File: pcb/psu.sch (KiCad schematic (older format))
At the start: 8 parts, among them J1 CONN_INTEGRALSTICK_FPGA_DEVICE, J2 CONN_INTEGRALSTICK_MCU_DEVICE, U1 STM32F777NIH6‎, U2 XC7A50T-1FTG256C, U7 LTC3374-QFN

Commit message: Finished initial schematic. Pin assignments will likely change during routing. Ready for test point insertion and signoff review.
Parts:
- added C107, C114, C117: 47 uF, symbol device:C
- added C108, C109, C110, C112: 22 uF, symbol device:C
- added C111, C113, C115: 10 uF, symbol device:C
- added C116: 100 uF, symbol device:C
- added L1: SPM6530T-2R2M, symbol passive-azonenberg:INDUCTOR_PWROUT
- added L2: NR6028T2R2N, symbol passive-azonenberg:INDUCTOR_PWROUT
- added L3, L4, L5: NRS5030T2R2NMGJ, symbol passive-azonenberg:INDUCTOR_PWROUT
- added R26: 1K, symbol device:R
- added R29, R30, R31, R32, R33: 0, symbol device:R
- added R34: 255K, symbol device:R
- added R35: 232K, symbol device:R
- added R36: 806K, symbol device:R
- added R37, R38, R39: 1.02M, symbol device:R
- added R40: 464K, symbol device:R
- added R41: 649K, symbol device:R
- added R42: 475K, symbol device:R
- added R43: 324K, symbol device:R
- added TP2, TP3: TESTPAD, symbol conn:CONN_01X01
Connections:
- net 1V0: now also C116.1, L1.1, R29.2
- net 1V8: now also C110.1, L4.1, R31.2
- net 2V5: now also C108.1, L5.1, R32.2
- net 3V3: now also C114.1, L2.1, R26.1, R33.2
- net 5V0: now also U7.11 (VIN4), U7.13 (EN4), U7.17 (RT), U7.18 (EN6), U7.2 (VIN1), U7.20 (FB5), U7.21 (VIN5), U7.24 (VIN6), U7.27 (VIN7), U7.30 (VIN8), U7.32 (EN8), U7.33 (EN7), U7.34 (MODE), U7.35 (VCC), U7.38 (EN1), U7.5 (VIN2), U7.6 (FB2), U7.7 (FB3), U7.8 (VIN3), C107.1, C109.1, C111.1, C113.1, C115.1, C117.1
- net GND: now also U7.14 (EN3), U7.16 (SYNC), U7.19 (EN5), U7.37 (EN2), U7.PAD (GND), C107.2, C108.2, C109.2, C110.2, C111.2, C112.2, C113.2, C114.2, C115.2, C116.2, C117.2, R39.1, R40.1, R41.1, R42.1, R43.1
- net 1V0_FB: now reaches U7.1 (FB1)
- net 1V0_FB: now also R34.1, R39.2
- net 1V0_SW: now reaches U7.3 (SW1)
- net 1V0_SW: now also U7.4 (SW2), U7.9 (SW3), L1.2
- net 3V3_SW: now reaches U7.10 (SW4)
- net 3V3_SW: now also U7.22 (SW5), L2.2
- net 3V3_FB: now reaches U7.12 (FB4)
- net 3V3_FB: now also R38.1, R43.2
- net 1V2_SW: now reaches U7.23 (SW6)
- net 1V2_SW: now also L3.2
- net 1V2_FB: now reaches U7.25 (FB6)
- net 1V2_FB: now also R35.1, R40.2
- net 1V8_FB: now reaches U7.26 (FB7)
- net 1V8_FB: now also R36.1, R41.2
- net 1V8_SW: now reaches U7.28 (SW7)
- net 1V8_SW: now also L4.2
- net 2V5_SW: now reaches U7.29 (SW8)
- net 2V5_SW: now also L5.2
- net 2V5_FB: now reaches U7.31 (FB8)
- net 2V5_FB: now also R37.1, R42.2
- net PGOOD: now reaches U7.15 (PGOOD_ALL)
- net PGOOD: now also R26.2, TP2.1 (P1)
- net PSU_TEMP: now reaches U7.36 (TEMP)
- net PSU_TEMP: now also TP3.1 (P1)
- new net 1V0_SENSE: R29.1, R34.2
- new net 1V2: C112.1, L3.1, R30.2
- new net 1V2_SENSE: R30.1, R35.2
- new net 1V8_SENSE: R31.1, R36.2
- new net 2V5_SENSE: R32.1, R37.2
- new net 3V3_SENSE: R33.1, R38.2
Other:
- note added: "PCB bulk input cap (reduce input ripple)"
- note added: "Remote sense and feedback for power rails"
- note added: "SMPS input caps"
- note added: "SMPS output caps"
- note added: "for 1V0"
- note added: "for 1V2"
- note added: "for 1V8"
- note added: "for 2V5"
- note added: "for 3V3"
- note removed: "TODO: SMPS stuff"

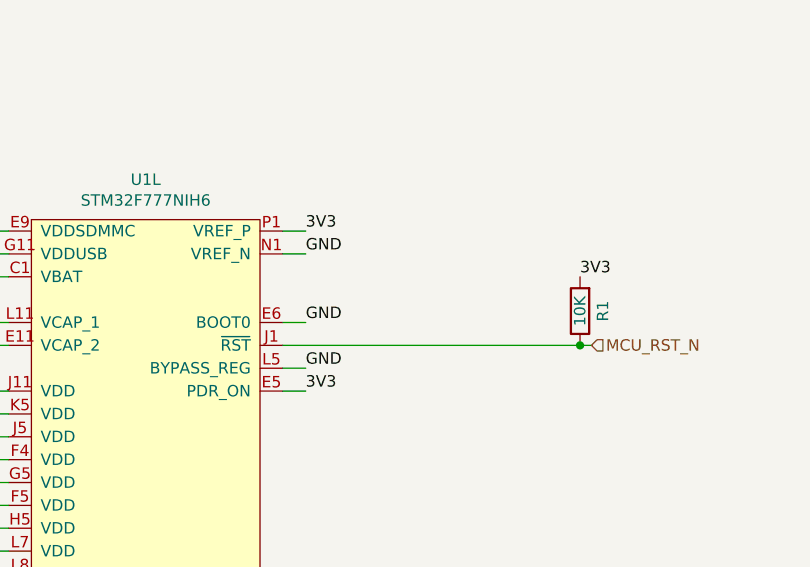
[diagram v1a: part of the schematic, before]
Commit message: Added pulldown to BOOT0 on MCU, brought it out to previously unused connector pin
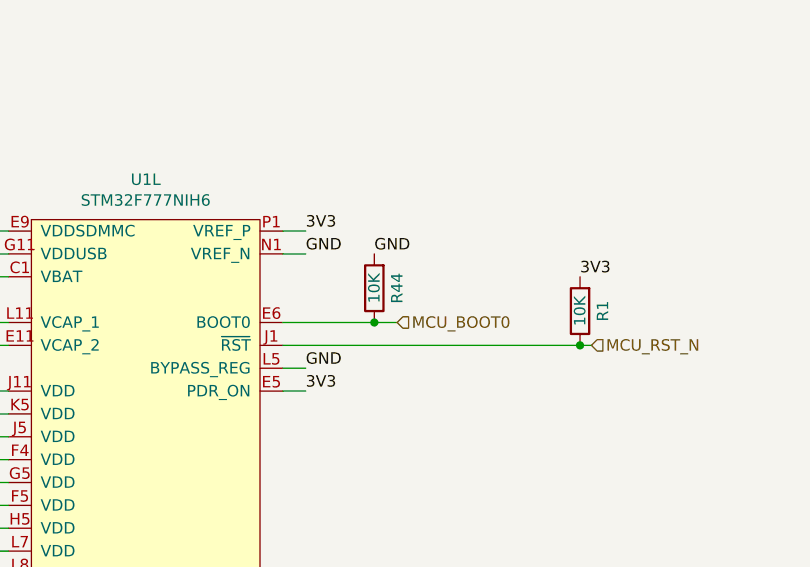
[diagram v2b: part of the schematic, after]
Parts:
- added R44: 10K, symbol device:R
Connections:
- net GND: now also R44.2; no longer U1.E6 (BOOT0)
- new net MCU_BOOT0: R44.1, U1.E6 (BOOT0)
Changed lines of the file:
@@
 Wire Wire Line
 	8400 8050 8300 8050
-Text Label 8400 8350 0    50   ~ 0
-GND
 Text HLabel 9650 8450 2    50   Input ~ 0
 MCU_RST_N
@@
 Text Label 8400 8650 0    50   ~ 0
 3V3
-Wire Wire Line
-	8400 8350 8300 8350
 Wire Wire Line
 	8400 8550 8300 8550
@@
 Wire Wire Line
 	7700 3300 7100 3300
+Text HLabel 8800 8350 2    50   Input ~ 0
+MCU_BOOT0
+$Comp
+L device:R R44
+U 1 1 5CFC62C6
+P 8700 8200
+F 0 "R44" V 8600 8200 50  0000 C CNN
+F 1 "10K" V 8700 8200 50  0000 C CNN
+F 2 "" V 8630 8200 50  0001 C CNN
+F 3 "" H 8700 8200 50  0001 C CNN
+	1    8700 8200
+	-1   0    0    1
+$EndComp
+Wire Wire Line
+	8300 8350 8700 8350
+Connection ~ 8700 8350
+Wire Wire Line
+	8700 8350 8800 8350
+Text Label 8700 8050 0    50   ~ 0
+GND
 $EndSCHEMATC

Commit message: Added capacitor for bbRAM on STM32. Removed MCU config oscillator, we now use the FPGA or internal oscillator as clock. Added SPI bus from FPGA to MCU.
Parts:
- added C46: CPH3225A-2K, symbol device:CP1
- added D2: CTS520,L3F‎, symbol device:D_Schottky
- added R45: 330, symbol device:R
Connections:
- net 3V3: now also D2.2 (A); no longer U1.C1 (VBAT)
- net GND: now also C46.2
- new net: D2.1 (K), R45.1
- new net MCU_VBAT: C46.1, R45.2, U1.C1 (VBAT)
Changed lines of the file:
@@
 Wire Wire Line
 	7000 7950 7100 7950
-Wire Wire Line
-	7000 8150 7100 8150
 $Comp
 L device:C C1
@@
 Wire Wire Line
 	7000 7950 7000 8050
-Connection ~ 7000 8050
-Wire Wire Line
-	7000 8050 7000 8150
 $Comp
 L device:C C2
@@
 Text Label 8700 8050 0    50   ~ 0
 GND
+Text Label 7000 8150 2    50   ~ 0
+MCU_VBAT
+Wire Wire Line
+	7000 8150 7100 8150
+Text Label 7900 6550 2    50   ~ 0
+MCU_VBAT
+$Comp
+L device:R R45
+U 1 1 5D0C77C0
+P 8000 6350
+F 0 "R45" H 8070 6396 50  0000 L CNN
+F 1 "330" H 8070 6305 50  0000 L CNN
+F 2 "" V 7930 6350 50  0001 C CNN
+F 3 "" H 8000 6350 50  0001 C CNN
+	1    8000 6350
+	1    0    0    -1
+$EndComp
+$Comp
+L device:CP1 C46
+U 1 1 5D0C7C66
+P 8000 6750
+F 0 "C46" H 8115 6796 50  0000 L CNN
+F 1 "CPH3225A-2K" H 8115 6705 50  0000 L CNN
+F 2 "" H 8000 6750 50  0001 C CNN
+F 3 "" H 8000 6750 50  0001 C CNN
+	1    8000 6750
+	1    0    0    -1
+$EndComp
+Wire Wire Line
+	8000 6500 8000 6550
+Wire Wire Line
+	7900 6550 8000 6550
+Connection ~ 8000 6550
+Wire Wire Line
+	8000 6550 8000 6600
+Text Label 7900 6900 2    50   ~ 0
+GND
+Wire Wire Line
+	7900 6900 8000 6900
+Text Label 7900 5900 2    50   ~ 0
+3V3
+$Comp
+L device:D_Schottky D2
+U 1 1 5D1CE534
+P 8000 6050
+F 0 "D2" V 8046 5971 50  0000 R CNN
+F 1 "CTS520,L3F‎" V 7955 5971 50  0000 R CNN
+F 2 "" H 8000 6050 50  0001 C CNN
+F 3 "" H 8000 6050 50  0001 C CNN
+	1    8000 6050
+	0    -1   -1   0
+$EndComp
+Wire Wire Line
+	7900 5900 8000 5900
 $EndSCHEMATC

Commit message: Assigned lots of footprints. Still have a few to go.
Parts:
- C1, C2: footprint (none) -> azonenberg_pcb:EIA_0603_CAP_NOSILK
- C107, C114, C116, C117: footprint (none) -> azonenberg_pcb:EIA_1210_CAP_NOSILK
- C108, C109, C110, C111, C112, C113, C115: footprint (none) -> azonenberg_pcb:EIA_1206_CAP_NOSILK
- L1, L2, L3, L4, L5, R1, R26, R29, R30, R31, R32, R33, R34, R35, R36, R37, R38, R39, R40, R41, R42, R43, R44, R45: footprint (none) -> azonenberg_pcb:EIA_0402_RES_NOSILK
- TP2, TP3: footprint (none) -> azonenberg_pcb:TESTPOINT_SMT_0.5MM
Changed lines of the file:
@@
 F 0 "C1" H 6565 8246 50  0000 L CNN
 F 1 "2.2 uF" H 6565 8155 50  0000 L CNN
-F 2 "" H 6488 8050 50  0001 C CNN
+F 2 "azonenberg_pcb:EIA_0603_CAP_NOSILK" H 6488 8050 50  0001 C CNN
 F 3 "" H 6450 8200 50  0001 C CNN
 	1    6450 8200
@@
 F 0 "C2" H 6565 8646 50  0000 L CNN
 F 1 "2.2 uF" H 6565 8555 50  0000 L CNN
-F 2 "" H 6488 8450 50  0001 C CNN
+F 2 "azonenberg_pcb:EIA_0603_CAP_NOSILK" H 6488 8450 50  0001 C CNN
 F 3 "" H 6450 8600 50  0001 C CNN
 	1    6450 8600
@@
 F 0 "R1" V 9500 8300 50  0000 C CNN
 F 1 "10K" V 9600 8300 50  0000 C CNN
-F 2 "" V 9530 8300 50  0001 C CNN
+F 2 "azonenberg_pcb:EIA_0402_RES_NOSILK" V 9530 8300 50  0001 C CNN
 F 3 "" H 9600 8300 50  0001 C CNN
 	1    9600 8300
@@
 F 0 "R26" H 4720 6346 50  0000 L CNN
 F 1 "1K" H 4720 6255 50  0000 L CNN
-F 2 "" V 4580 6300 50  0001 C CNN
+F 2 "azonenberg_pcb:EIA_0402_RES_NOSILK" V 4580 6300 50  0001 C CNN
 F 3 "" H 4650 6300 50  0001 C CNN
 	1    4650 6300
@@
 F 0 "TP2" H 5128 6491 50  0000 L CNN
 F 1 "TESTPAD" H 5128 6400 50  0000 L CNN
-F 2 "" H 5050 6450 50  0001 C CNN
+F 2 "azonenberg_pcb:TESTPOINT_SMT_0.5MM" H 5050 6450 50  0001 C CNN
 F 3 "" H 5050 6450 50  0001 C CNN
 	1    5050 6450
@@
 F 0 "TP3" H 5128 6791 50  0000 L CNN
 F 1 "TESTPAD" H 5128 6700 50  0000 L CNN
-F 2 "" H 5050 6750 50  0001 C CNN
+F 2 "azonenberg_pcb:TESTPOINT_SMT_0.5MM" H 5050 6750 50  0001 C CNN
 F 3 "" H 5050 6750 50  0001 C CNN
 	1    5050 6750
@@
 F 0 "L1" V 1993 1150 40  0000 C CNN
 F 1 "SPM6530T-2R2M" V 1917 1150 40  0000 C CNN
-F 2 "" H 1800 1150 60  0000 C CNN
+F 2 "azonenberg_pcb:EIA_0402_RES_NOSILK" H 1800 1150 60  0001 C CNN
 F 3 "" H 1800 1150 60  0000 C CNN
 	1    1800 1150
@@
 F 0 "L5" V 1993 5750 40  0000 C CNN
 F 1 "NRS5030T2R2NMGJ" V 1917 5750 40  0000 C CNN
-F 2 "" H 1800 5750 60  0000 C CNN
+F 2 "azonenberg_pcb:EIA_0402_RES_NOSILK" H 1800 5750 60  0001 C CNN
 F 3 "" H 1800 5750 60  0000 C CNN
 	1    1800 5750
@@
 F 0 "L4" V 1993 5150 40  0000 C CNN
 F 1 "NRS5030T2R2NMGJ" V 1917 5150 40  0000 C CNN
-F 2 "" H 1800 5150 60  0000 C CNN
+F 2 "azonenberg_pcb:EIA_0402_RES_NOSILK" H 1800 5150 60  0001 C CNN
 F 3 "" H 1800 5150 60  0000 C CNN
 	1    1800 5150
@@
 F 0 "L3" V 1993 4500 40  0000 C CNN
 F 1 "NRS5030T2R2NMGJ" V 1917 4500 40  0000 C CNN
-F 2 "" H 1800 4500 60  0000 C CNN
+F 2 "azonenberg_pcb:EIA_0402_RES_NOSILK" H 1800 4500 60  0001 C CNN
 F 3 "" H 1800 4500 60  0000 C CNN
 	1    1800 4500
@@
 F 0 "L2" V 1993 3200 40  0000 C CNN
 F 1 "NR6028T2R2N" V 1917 3200 40  0000 C CNN
-F 2 "" H 1800 3200 60  0000 C CNN
+F 2 "azonenberg_pcb:EIA_0402_RES_NOSILK" H 1800 3200 60  0001 C CNN
 F 3 "" H 1800 3200 60  0000 C CNN
 	1    1800 3200
@@
 F 0 "R29" V 6050 1300 50  0000 C CNN
 F 1 "0" V 6000 1100 50  0000 C CNN
-F 2 "" V 5930 1100 50  0001 C CNN
+F 2 "azonenberg_pcb:EIA_0402_RES_NOSILK" V 5930 1100 50  0001 C CNN
 F 3 "" H 6000 1100 50  0001 C CNN
 	1    6000 1100
@@
 F 0 "R39" V 7700 1300 50  0000 C CNN
 F 1 "1.02M" V 7650 1100 50  0000 C CNN
-F 2 "" V 7580 1100 50  0001 C CNN
+F 2 "azonenberg_pcb:EIA_0402_RES_NOSILK" V 7580 1100 50  0001 C CNN
 F 3 "" H 7650 1100 50  0001 C CNN
 	1    7650 1100
@@
 F 0 "R34" V 7000 1300 50  0000 C CNN
 F 1 "255K" V 6950 1100 50  0000 C CNN
-F 2 "" V 6880 1100 50  0001 C CNN
+F 2 "azonenberg_pcb:EIA_0402_RES_NOSILK" V 6880 1100 50  0001 C CNN
 F 3 "" H 6950 1100 50  0001 C CNN
 	1    6950 1100
@@
 F 0 "R30" V 6050 1450 50  0000 C CNN
 F 1 "0" V 6000 1250 50  0000 C CNN
-F 2 "" V 5930 1250 50  0001 C CNN
+F 2 "azonenberg_pcb:EIA_0402_RES_NOSILK" V 5930 1250 50  0001 C CNN
 F 3 "" H 6000 1250 50  0001 C CNN
 	1    6000 1250
@@
 F 0 "R40" V 7700 1450 50  0000 C CNN
 F 1 "464K" V 7650 1250 50  0000 C CNN
-F 2 "" V 7580 1250 50  0001 C CNN
+F 2 "azonenberg_pcb:EIA_0402_RES_NOSILK" V 7580 1250 50  0001 C CNN
 F 3 "" H 7650 1250 50  0001 C CNN
 	1    7650 1250
@@
 F 0 "R35" V 7000 1450 50  0000 C CNN
 F 1 "232K" V 6950 1250 50  0000 C CNN
-F 2 "" V 6880 1250 50  0001 C CNN
+F 2 "azonenberg_pcb:EIA_0402_RES_NOSILK" V 6880 1250 50  0001 C CNN
 F 3 "" H 6950 1250 50  0001 C CNN
 	1    6950 1250
@@
 F 0 "R31" V 6050 1600 50  0000 C CNN
 F 1 "0" V 6000 1400 50  0000 C CNN
-F 2 "" V 5930 1400 50  0001 C CNN
+F 2 "azonenberg_pcb:EIA_0402_RES_NOSILK" V 5930 1400 50  0001 C CNN
 F 3 "" H 6000 1400 50  0001 C CNN
 	1    6000 1400
@@
 F 0 "R41" V 7700 1600 50  0000 C CNN
 F 1 "649K" V 7650 1400 50  0000 C CNN
-F 2 "" V 7580 1400 50  0001 C CNN
+F 2 "azonenberg_pcb:EIA_0402_RES_NOSILK" V 7580 1400 50  0001 C CNN
 F 3 "" H 7650 1400 50  0001 C CNN
 	1    7650 1400
@@
 F 0 "R36" V 7000 1600 50  0000 C CNN
 F 1 "806K" V 6950 1400 50  0000 C CNN
-F 2 "" V 6880 1400 50  0001 C CNN
+F 2 "azonenberg_pcb:EIA_0402_RES_NOSILK" V 6880 1400 50  0001 C CNN
 F 3 "" H 6950 1400 50  0001 C CNN
 	1    6950 1400
@@
 F 0 "R32" V 6050 1750 50  0000 C CNN
 F 1 "0" V 6000 1550 50  0000 C CNN
-F 2 "" V 5930 1550 50  0001 C CNN
+F 2 "azonenberg_pcb:EIA_0402_RES_NOSILK" V 5930 1550 50  0001 C CNN
 F 3 "" H 6000 1550 50  0001 C CNN
 	1    6000 1550
@@
 F 0 "R42" V 7700 1750 50  0000 C CNN
 F 1 "475K" V 7650 1550 50  0000 C CNN
-F 2 "" V 7580 1550 50  0001 C CNN
+F 2 "azonenberg_pcb:EIA_0402_RES_NOSILK" V 7580 1550 50  0001 C CNN
 F 3 "" H 7650 1550 50  0001 C CNN
 	1    7650 1550
@@
 F 0 "R37" V 7000 1750 50  0000 C CNN
 F 1 "1.02M" V 6950 1550 50  0000 C CNN
-F 2 "" V 6880 1550 50  0001 C CNN
+F 2 "azonenberg_pcb:EIA_0402_RES_NOSILK" V 6880 1550 50  0001 C CNN
 F 3 "" H 6950 1550 50  0001 C CNN
 	1    6950 1550
@@
 F 0 "R33" V 6050 1900 50  0000 C CNN
 F 1 "0" V 6000 1700 50  0000 C CNN
-F 2 "" V 5930 1700 50  0001 C CNN
+F 2 "azonenberg_pcb:EIA_0402_RES_NOSILK" V 5930 1700 50  0001 C CNN
 F 3 "" H 6000 1700 50  0001 C CNN
 	1    6000 1700
@@
 F 0 "R43" V 7700 1900 50  0000 C CNN
 F 1 "324K" V 7650 1700 50  0000 C CNN
-F 2 "" V 7580 1700 50  0001 C CNN
+F 2 "azonenberg_pcb:EIA_0402_RES_NOSILK" V 7580 1700 50  0001 C CNN
 F 3 "" H 7650 1700 50  0001 C CNN
 	1    7650 1700
@@
 F 0 "R38" V 7000 1900 50  0000 C CNN
 F 1 "1.02M" V 6950 1700 50  0000 C CNN
-F 2 "" V 6880 1700 50  0001 C CNN
+F 2 "azonenberg_pcb:EIA_0402_RES_NOSILK" V 6880 1700 50  0001 C CNN
 F 3 "" H 6950 1700 50  0001 C CNN
 	1    6950 1700
@@
 F 0 "C107" H 6015 2496 50  0000 L CNN
 F 1 "47 uF" H 6015 2405 50  0000 L CNN
-F 2 "" H 5938 2300 50  0001 C CNN
+F 2 "azonenberg_pcb:EIA_1210_CAP_NOSILK" H 5938 2300 50  0001 C CNN
 F 3 "" H 5900 2450 50  0001 C CNN
 	1    5900 2450
@@
 F 0 "C109" H 6615 2496 50  0000 L CNN
 F 1 "22 uF" H 6615 2405 50  0000 L CNN
-F 2 "" H 6538 2300 50  0001 C CNN
+F 2 "azonenberg_pcb:EIA_1206_CAP_NOSILK" H 6538 2300 50  0001 C CNN
 F 3 "" H 6500 2450 50  0001 C CNN
 	1    6500 2450
@@
 F 0 "C111" H 7215 2496 50  0000 L CNN
 F 1 "10 uF" H 7215 2405 50  0000 L CNN
-F 2 "" H 7138 2300 50  0001 C CNN
+F 2 "azonenberg_pcb:EIA_1206_CAP_NOSILK" H 7138 2300 50  0001 C CNN
 F 3 "" H 7100 2450 50  0001 C CNN
 	1    7100 2450
@@
 F 0 "C113" H 7815 2496 50  0000 L CNN
 F 1 "10 uF" H 7815 2405 50  0000 L CNN
-F 2 "" H 7738 2300 50  0001 C CNN
+F 2 "azonenberg_pcb:EIA_1206_CAP_NOSILK" H 7738 2300 50  0001 C CNN
 F 3 "" H 7700 2450 50  0001 C CNN
 	1    7700 2450
@@
 F 0 "C115" H 8315 2496 50  0000 L CNN
 F 1 "10 uF" H 8315 2405 50  0000 L CNN
-F 2 "" H 8238 2300 50  0001 C CNN
+F 2 "azonenberg_pcb:EIA_1206_CAP_NOSILK" H 8238 2300 50  0001 C CNN
 F 3 "" H 8200 2450 50  0001 C CNN
 	1    8200 2450
@@
 F 0 "C117" H 9415 2496 50  0000 L CNN
 F 1 "47 uF" H 9415 2405 50  0000 L CNN
-F 2 "" H 9338 2300 50  0001 C CNN
+F 2 "azonenberg_pcb:EIA_1210_CAP_NOSILK" H 9338 2300 50  0001 C CNN
 F 3 "" H 9300 2450 50  0001 C CNN
 	1    9300 2450
@@
 F 0 "C108" H 6015 3196 50  0000 L CNN
 F 1 "22 uF" H 6015 3105 50  0000 L CNN
-F 2 "" H 5938 3000 50  0001 C CNN
+F 2 "azonenberg_pcb:EIA_1206_CAP_NOSILK" H 5938 3000 50  0001 C CNN
 F 3 "" H 5900 3150 50  0001 C CNN
 	1    5900 3150
@@
 F 0 "C110" H 6615 3196 50  0000 L CNN
 F 1 "22 uF" H 6615 3105 50  0000 L CNN
-F 2 "" H 6538 3000 50  0001 C CNN
+F 2 "azonenberg_pcb:EIA_1206_CAP_NOSILK" H 6538 3000 50  0001 C CNN
 F 3 "" H 6500 3150 50  0001 C CNN
 	1    6500 3150
@@
 F 0 "C112" H 7215 3196 50  0000 L CNN
 F 1 "22 uF" H 7215 3105 50  0000 L CNN
-F 2 "" H 7138 3000 50  0001 C CNN
+F 2 "azonenberg_pcb:EIA_1206_CAP_NOSILK" H 7138 3000 50  0001 C CNN
 F 3 "" H 7100 3150 50  0001 C CNN
 	1    7100 3150
@@
 F 0 "C114" H 7815 3196 50  0000 L CNN
 F 1 "47 uF" H 7815 3105 50  0000 L CNN
-F 2 "" H 7738 3000 50  0001 C CNN
+F 2 "azonenberg_pcb:EIA_1210_CAP_NOSILK" H 7738 3000 50  0001 C CNN
 F 3 "" H 7700 3150 50  0001 C CNN
 	1    7700 3150
@@
 F 0 "C116" H 8315 3196 50  0000 L CNN
 F 1 "100 uF" H 8315 3105 50  0000 L CNN
-F 2 "" H 8238 3000 50  0001 C CNN
+F 2 "azonenberg_pcb:EIA_1210_CAP_NOSILK" H 8238 3000 50  0001 C CNN
 F 3 "" H 8200 3150 50  0001 C CNN
 	1    8200 3150
@@
 F 0 "R44" V 8600 8200 50  0000 C CNN
 F 1 "10K" V 8700 8200 50  0000 C CNN
-F 2 "" V 8630 8200 50  0001 C CNN
+F 2 "azonenberg_pcb:EIA_0402_RES_NOSILK" V 8630 8200 50  0001 C CNN
 F 3 "" H 8700 8200 50  0001 C CNN
 	1    8700 8200
@@
 F 0 "R45" H 8070 6396 50  0000 L CNN
 F 1 "330" H 8070 6305 50  0000 L CNN
-F 2 "" V 7930 6350 50  0001 C CNN
+F 2 "azonenberg_pcb:EIA_0402_RES_NOSILK" V 7930 6350 50  0001 C CNN
 F 3 "" H 8000 6350 50  0001 C CNN
 	1    8000 6350

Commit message: Assigned inductor footprints
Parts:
- L1: footprint azonenberg_pcb:EIA_0402_RES_NOSILK -> azonenberg_pcb:INDUCTOR_TDK_SPM6530
- L2: footprint azonenberg_pcb:EIA_0402_RES_NOSILK -> azonenberg_pcb:INDUCTOR_YUDEN_NR6028
- L3, L4, L5: footprint azonenberg_pcb:EIA_0402_RES_NOSILK -> azonenberg_pcb:INDUCTOR_YUDEN_NRS5030
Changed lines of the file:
@@
 F 0 "L1" V 1993 1150 40  0000 C CNN
 F 1 "SPM6530T-2R2M" V 1917 1150 40  0000 C CNN
-F 2 "azonenberg_pcb:EIA_0402_RES_NOSILK" H 1800 1150 60  0001 C CNN
+F 2 "azonenberg_pcb:INDUCTOR_TDK_SPM6530" H 1800 1150 60  0001 C CNN
 F 3 "" H 1800 1150 60  0000 C CNN
 	1    1800 1150
@@
 F 0 "L5" V 1993 5750 40  0000 C CNN
 F 1 "NRS5030T2R2NMGJ" V 1917 5750 40  0000 C CNN
-F 2 "azonenberg_pcb:EIA_0402_RES_NOSILK" H 1800 5750 60  0001 C CNN
+F 2 "azonenberg_pcb:INDUCTOR_YUDEN_NRS5030" H 1800 5750 60  0001 C CNN
 F 3 "" H 1800 5750 60  0000 C CNN
 	1    1800 5750
@@
 F 0 "L4" V 1993 5150 40  0000 C CNN
 F 1 "NRS5030T2R2NMGJ" V 1917 5150 40  0000 C CNN
-F 2 "azonenberg_pcb:EIA_0402_RES_NOSILK" H 1800 5150 60  0001 C CNN
+F 2 "azonenberg_pcb:INDUCTOR_YUDEN_NRS5030" H 1800 5150 60  0001 C CNN
 F 3 "" H 1800 5150 60  0000 C CNN
 	1    1800 5150
@@
 F 0 "L3" V 1993 4500 40  0000 C CNN
 F 1 "NRS5030T2R2NMGJ" V 1917 4500 40  0000 C CNN
-F 2 "azonenberg_pcb:EIA_0402_RES_NOSILK" H 1800 4500 60  0001 C CNN
+F 2 "azonenberg_pcb:INDUCTOR_YUDEN_NRS5030" H 1800 4500 60  0001 C CNN
 F 3 "" H 1800 4500 60  0000 C CNN
 	1    1800 4500
@@
 F 0 "L2" V 1993 3200 40  0000 C CNN
 F 1 "NR6028T2R2N" V 1917 3200 40  0000 C CNN
-F 2 "azonenberg_pcb:EIA_0402_RES_NOSILK" H 1800 3200 60  0001 C CNN
+F 2 "azonenberg_pcb:INDUCTOR_YUDEN_NR6028" H 1800 3200 60  0001 C CNN
 F 3 "" H 1800 3200 60  0000 C CNN
 	1    1800 3200

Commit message: Finished initial footprint assignments
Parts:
- C46: footprint (none) -> azonenberg_pcb:CAP_SEIKO_CPH3225A
- D2: footprint (none) -> azonenberg_pcb:SOD882
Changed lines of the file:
@@
 F 0 "C46" H 8115 6796 50  0000 L CNN
 F 1 "CPH3225A-2K" H 8115 6705 50  0000 L CNN
-F 2 "" H 8000 6750 50  0001 C CNN
+F 2 "azonenberg_pcb:CAP_SEIKO_CPH3225A" H 8000 6750 50  0001 C CNN
 F 3 "" H 8000 6750 50  0001 C CNN
 	1    8000 6750
@@
 F 0 "D2" V 8046 5971 50  0000 R CNN
 F 1 "CTS520,L3F‎" V 7955 5971 50  0000 R CNN
-F 2 "" H 8000 6050 50  0001 C CNN
+F 2 "azonenberg_pcb:SOD882" H 8000 6050 50  0001 C CNN
 F 3 "" H 8000 6050 50  0001 C CNN
 	1    8000 6050

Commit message: Finished first iteration layout of RAM. Lots of pin swaps.
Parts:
- U2: footprint azonenberg_pcb:BGA_256_17x17_FULLARRAY_1MM -> azonenberg_pcb:BGA_256_17x17_FULLARRAY_1MM_0.4MM_FTG256
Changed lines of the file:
@@
 Sheet 2 8
 Title "INTEGRALSTICK Compute Module"
-Date "2018-11-09"
+Date "2018-11-11"
 Rev "0.1"
 Comp "Andrew D. Zonenberg"
@@
 F 0 "U2" H 13125 11197 60  0000 C CNN
 F 1 "XC7A50T-1FTG256C" H 13125 11091 60  0000 C CNN
-F 2 "azonenberg_pcb:BGA_256_17x17_FULLARRAY_1MM" H 12450 6050 60  0001 C CNN
+F 2 "azonenberg_pcb:BGA_256_17x17_FULLARRAY_1MM_0.4MM_FTG256" H 12450 6050 60  0001 C CNN
 F 3 "" H 12450 6050 60  0000 C CNN
 	2    12450 6050
